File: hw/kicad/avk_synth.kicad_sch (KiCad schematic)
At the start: 0 parts

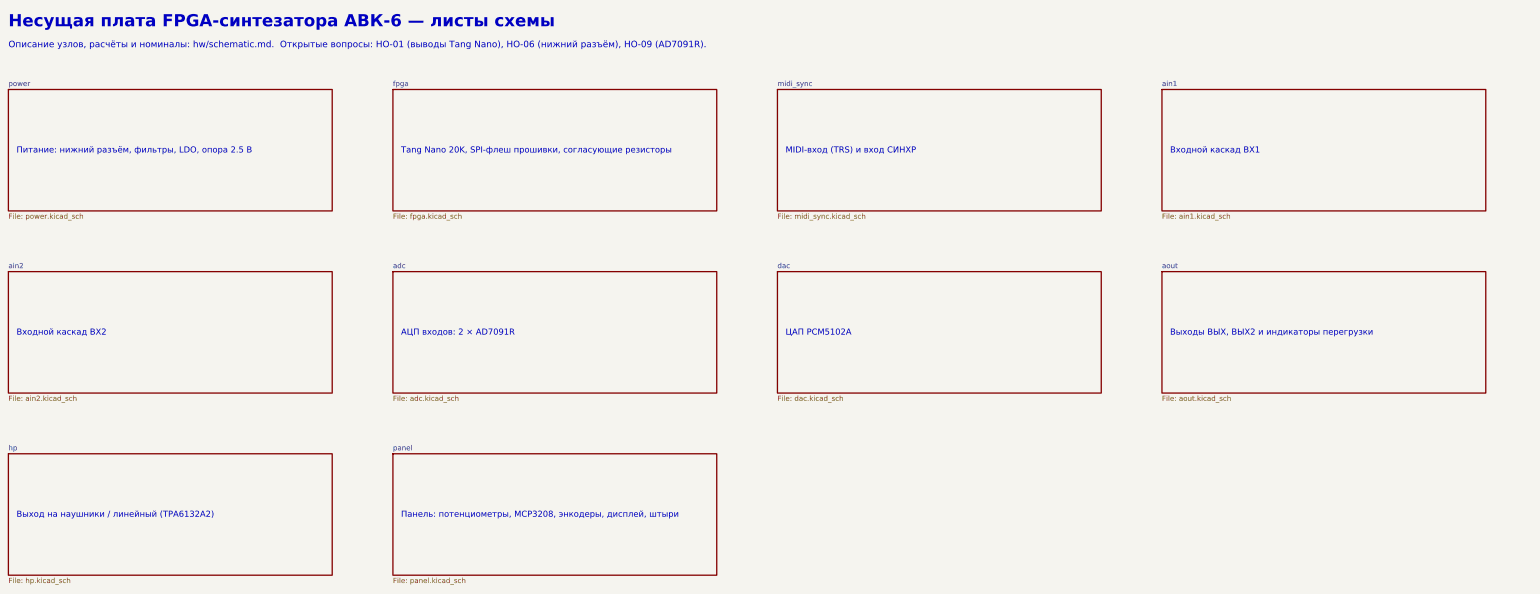
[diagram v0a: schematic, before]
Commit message: Reorganize KiCad schematic into 7 functional sheets with framed blocks
- Sheets: power, fpga, midi_sync, analog_in (inputs + ADC), audio_out
  (DAC + OUT/OUT2 + clip LEDs), phones, panel
- Each functional block is drawn in a dashed frame with a title; blocks are
  tiled across the sheet, A3/A2 chosen automatically
- Netlist check still 153/153; PDF and docs updated

Co-Authored-By: Claude Opus 5.5 <noreply@anthropic.com>
Claude-Session: https://claude.ai/code/session_01JcNV2ZCXWxtNzRVWffkrjk
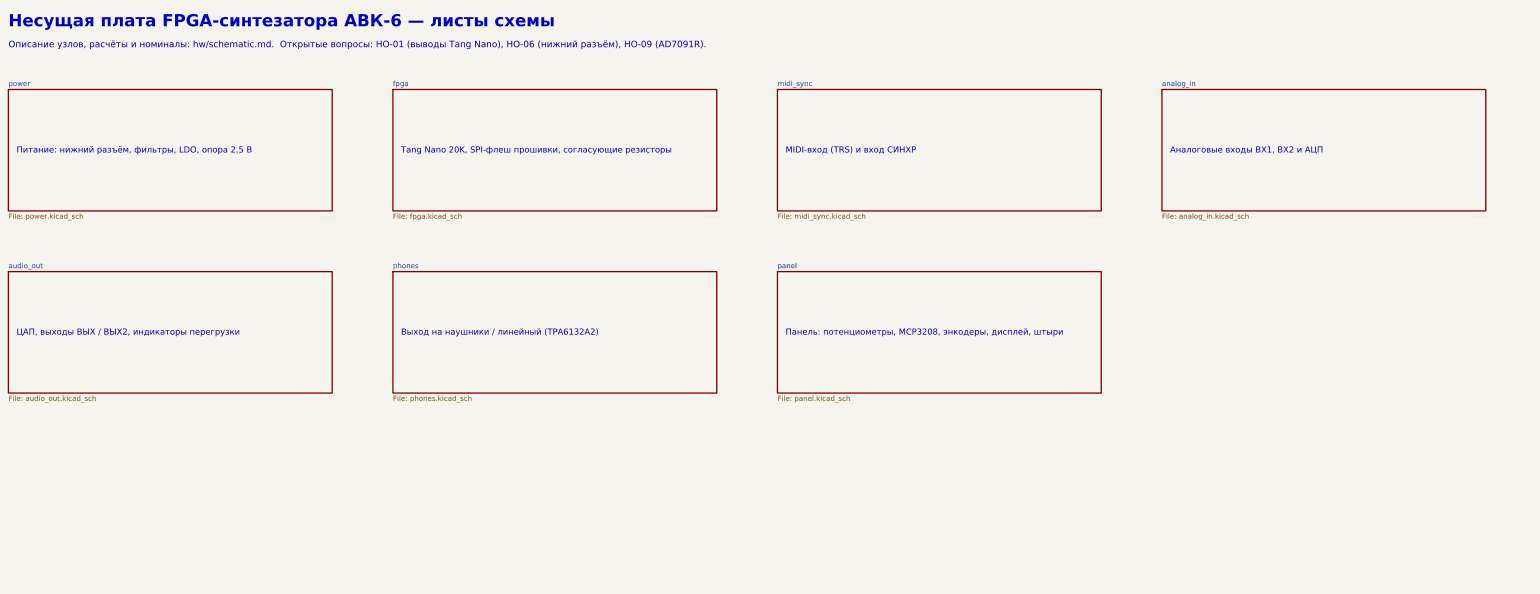
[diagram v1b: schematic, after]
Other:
- removed sheet adc
- removed sheet ain1
- removed sheet ain2
- removed sheet aout
- removed sheet dac
- removed sheet hp
- added sheet analog_in (analog_in.kicad_sch)
- added sheet audio_out (audio_out.kicad_sch)
- added sheet phones (phones.kicad_sch)
- note added: "Аналоговые входы ВХ1, ВХ2 и АЦП"
- note added: "ЦАП, выходы ВЫХ / ВЫХ2, индикаторы перегрузки"
- note removed: "АЦП входов: 2 × AD7091R"
- note removed: "Входной каскад ВХ1"
- note removed: "Входной каскад ВХ2"
- note removed: "Выходы ВЫХ, ВЫХ2 и индикаторы перегрузки"
- note removed: "ЦАП PCM5102A"
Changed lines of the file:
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@@
       (type solid))
     (fill (color 0 0 0 0))
-    (property "Sheetname" "ain1"
+    (property "Sheetname" "analog_in"
       (at 305 39.3 0)
       (effects
         (font (size 1.27 1.27))
         (justify left bottom)))
-    (property "Sheetfile" "ain1.kicad_sch"
+    (property "Sheetfile" "analog_in.kicad_sch"
       (at 305 70.6 0)
       (effects
@@
       (project "avk_synth"
         (path "/32f38c40-2b50-5c71-84ba-2b066e9f8d2d" (page "5")))))
-  (text "Входной каскад ВХ1"
+  (text "Аналоговые входы ВХ1, ВХ2 и АЦП"
     (at 307 56 0)
     (effects
@@
       (type solid))
     (fill (color 0 0 0 0))
-    (property "Sheetname" "ain2"
+    (property "Sheetname" "audio_out"
       (at 20 84.3 0)
       (effects
         (font (size 1.27 1.27))
         (justify left bottom)))
-    (property "Sheetfile" "ain2.kicad_sch"
+    (property "Sheetfile" "audio_out.kicad_sch"
       (at 20 115.6 0)
       (effects
@@
       (project "avk_synth"
         (path "/32f38c40-2b50-5c71-84ba-2b066e9f8d2d" (page "6")))))
-  (text "Входной каскад ВХ2"
+  (text "ЦАП, выходы ВЫХ / ВЫХ2, индикаторы перегрузки"
     (at 22 101 0)
     (effects
@@
       (type solid))
     (fill (color 0 0 0 0))
-    (property "Sheetname" "adc"
+    (property "Sheetname" "phones"
       (at 115 84.3 0)
       (effects
         (font (size 1.27 1.27))
         (justify left bottom)))
-    (property "Sheetfile" "adc.kicad_sch"
+    (property "Sheetfile" "phones.kicad_sch"
       (at 115 115.6 0)
       (effects
@@
       (project "avk_synth"
         (path "/32f38c40-2b50-5c71-84ba-2b066e9f8d2d" (page "7")))))
-  (text "АЦП входов: 2 × AD7091R"
+  (text "Выход на наушники / линейный (TPA6132A2)"
     (at 117 101 0)
     (effects
@@
       (type solid))
     (fill (color 0 0 0 0))
-    (property "Sheetname" "dac"
+    (property "Sheetname" "panel"
       (at 210 84.3 0)
       (effects
         (font (size 1.27 1.27))
         (justify left bottom)))
-    (property "Sheetfile" "dac.kicad_sch"
+    (property "Sheetfile" "panel.kicad_sch"
       (at 210 115.6 0)
       (effects
@@
       (project "avk_synth"
         (path "/32f38c40-2b50-5c71-84ba-2b066e9f8d2d" (page "8")))))
-  (text "ЦАП PCM5102A"
+  (text "Панель: потенциометры, MCP3208, энкодеры, дисплей, штыри"
     (at 212 101 0)
     (effects
       (font (size 1.5 1.5))
-      (justify left bottom))
-)
-  (sheet
-    (at 305 85)
-    (size 80 30)
-    (fields_autoplaced)
-    (stroke
-      (width 0.1524)
-      (type solid))
-    (fill (color 0 0 0 0))
-    (property "Sheetname" "aout"
-      (at 305 84.3 0)
-      (effects
-        (font (size 1.27 1.27))
-        (justify left bottom)))
-    (property "Sheetfile" "aout.kicad_sch"
-      (at 305 115.6 0)
-      (effects
-        (font (size 1.27 1.27))
-        (justify left top)))
-    (instances
-      (project "avk_synth"
-        (path "/32f38c40-2b50-5c71-84ba-2b066e9f8d2d" (page "9")))))
-  (text "Выходы ВЫХ, ВЫХ2 и индикаторы перегрузки"
-    (at 307 101 0)
-    (effects
-      (font (size 1.5 1.5))
-      (justify left bottom))
-)
-  (sheet
-    (at 20 130)
-    (size 80 30)
-    (fields_autoplaced)
-    (stroke
-      (width 0.1524)
-      (type solid))
-    (fill (color 0 0 0 0))
-    (property "Sheetname" "hp"
-      (at 20 129.3 0)
-      (effects
-        (font (size 1.27 1.27))
-        (justify left bottom)))
-    (property "Sheetfile" "hp.kicad_sch"
-      (at 20 160.6 0)
-      (effects
-        (font (size 1.27 1.27))
-        (justify left top)))
-    (instances
-      (project "avk_synth"
-        (path "/32f38c40-2b50-5c71-84ba-2b066e9f8d2d" (page "10")))))
-  (text "Выход на наушники / линейный (TPA6132A2)"
-    (at 22 146 0)
-    (effects
-      (font (size 1.5 1.5))
-      (justify left bottom))
-)
-  (sheet
-    (at 115 130)
-    (size 80 30)
-    (fields_autoplaced)
-    (stroke
-      (width 0.1524)
-      (type solid))
-    (fill (color 0 0 0 0))
-    (property "Sheetname" "panel"
-      (at 115 129.3 0)
-      (effects
-        (font (size 1.27 1.27))
-        (justify left bottom)))
-    (property "Sheetfile" "panel.kicad_sch"
-      (at 115 160.6 0)
-      (effects
-        (font (size 1.27 1.27))
-        (justify left top)))
-    (instances
-      (project "avk_synth"
-        (path "/32f38c40-2b50-5c71-84ba-2b066e9f8d2d" (page "11")))))
-  (text "Панель: потенциометры, MCP3208, энкодеры, дисплей, штыри"
-    (at 117 146 0)
-    (effects
-      (font (size 1.5 1.5))
